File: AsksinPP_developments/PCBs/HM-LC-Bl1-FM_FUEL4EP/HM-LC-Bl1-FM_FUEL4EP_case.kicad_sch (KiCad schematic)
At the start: 34 parts, among them J1 Down button, J11 24V PSU, J12 230V supply relais, J13 Velux Motor, J14 Motor direction LEDs, J15 charge indication LED, J16 Cold_Device_Socket, J2 Up Button, J3 Dual LED, J4 Config Button, J6 Conn_01x02_Male, J7 LED rot, J8 LED grün, J9 LED gelb, M1 24V Velux Motor, SW1 Down Button, SW2 Down Button, SW3 Config Button

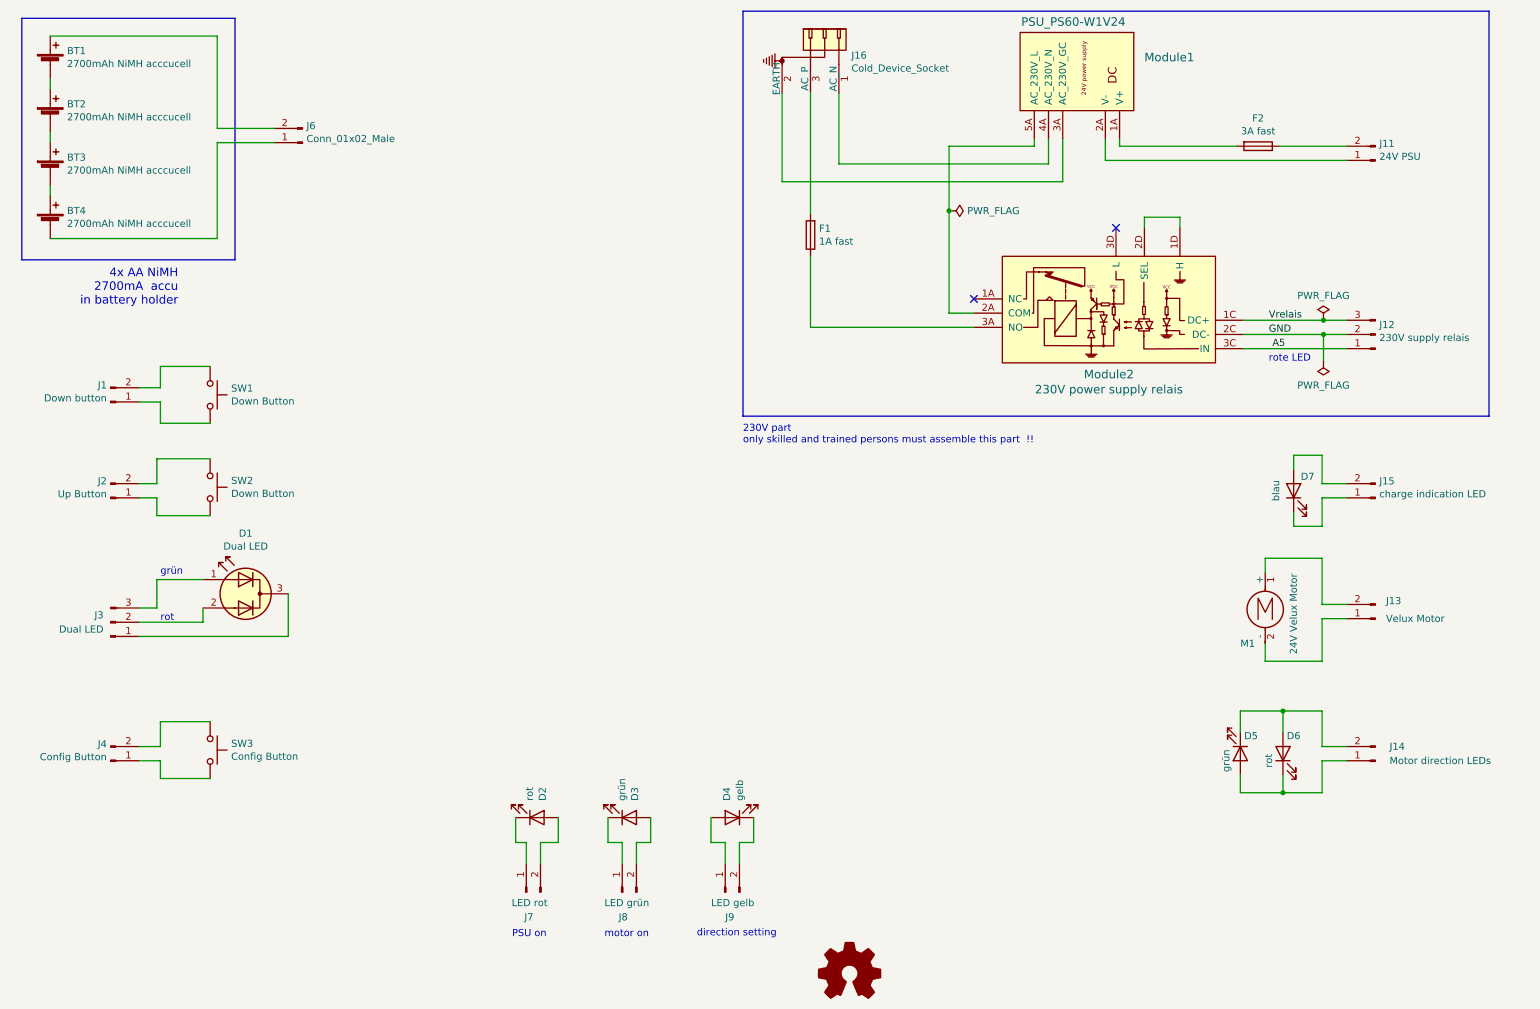
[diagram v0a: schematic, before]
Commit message: PCBs/HM-LC-Bl1-FM_FUEL4EP: migration to KiCAD 8
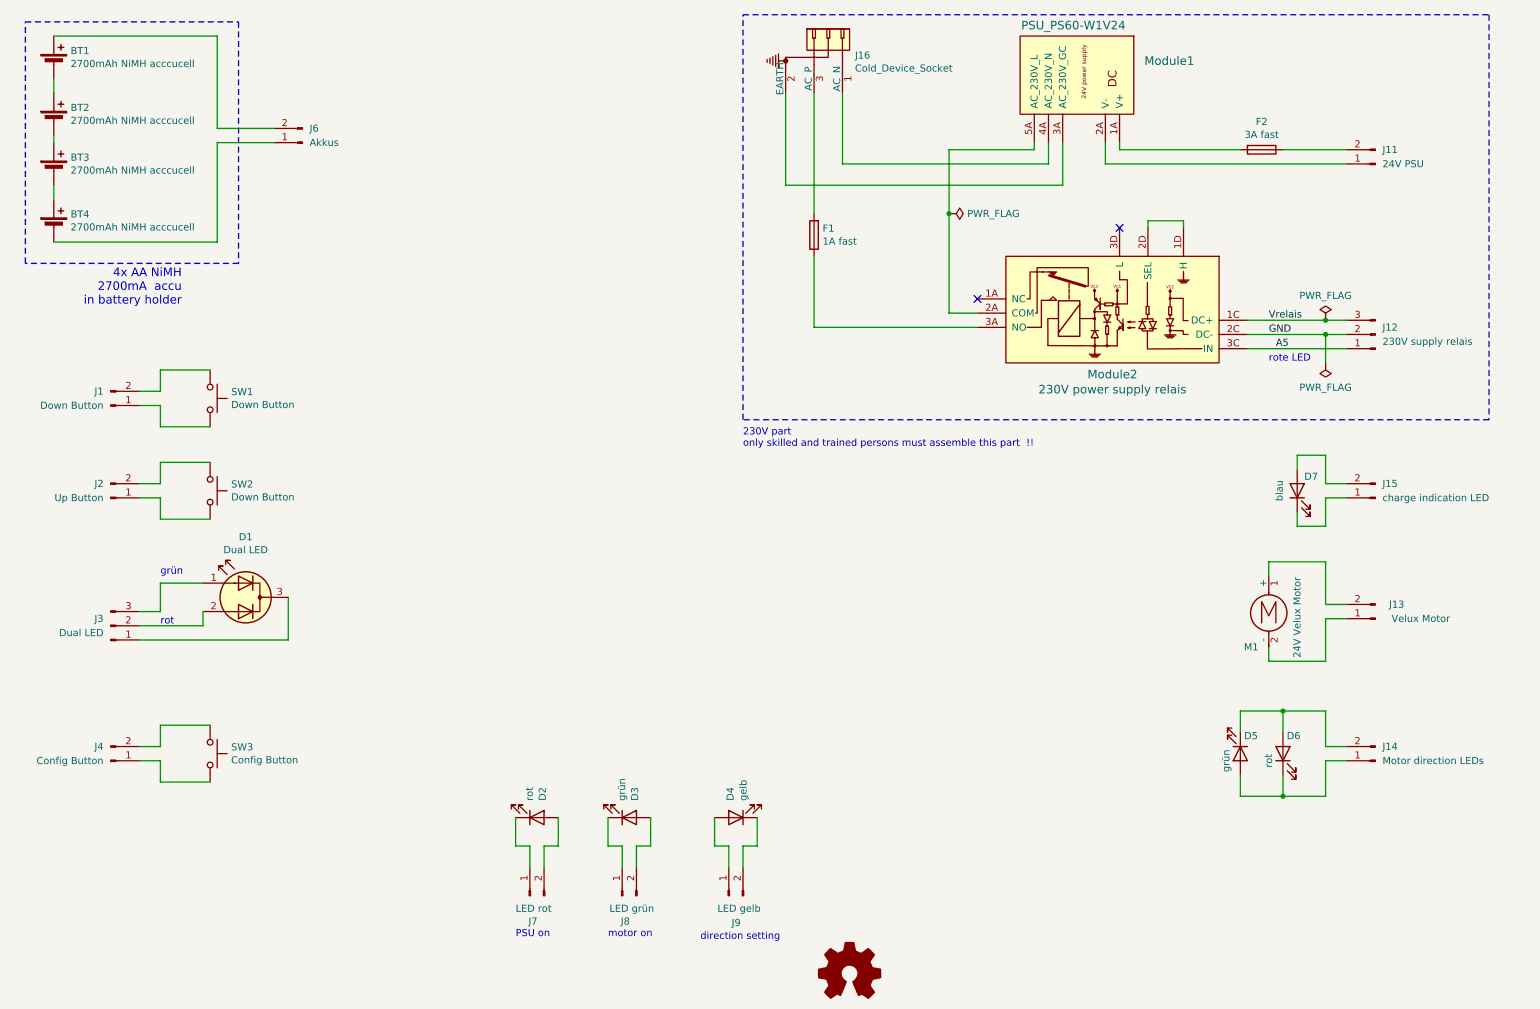
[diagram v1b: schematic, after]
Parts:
- removed J1: Down button, symbol Connector:Conn_01x02_Male
- removed J11: 24V PSU, symbol Connector:Conn_01x02_Male
- removed J12: 230V supply relais, symbol Connector:Conn_01x03_Male
- removed J13: Velux Motor, symbol Connector:Conn_01x02_Male
- removed J14: Motor direction LEDs, symbol Connector:Conn_01x02_Male
- removed J15: charge indication LED, symbol Connector:Conn_01x02_Male
- removed J2: Up Button, symbol Connector:Conn_01x02_Male
- removed J3: Dual LED, symbol Connector:Conn_01x03_Male
- removed J4: Config Button, symbol Connector:Conn_01x02_Male
- removed J6: Conn_01x02_Male, symbol Connector:Conn_01x02_Male
- removed J7: LED rot, symbol Connector:Conn_01x02_Male
- removed J8: LED grün, symbol Connector:Conn_01x02_Male
- removed J9: LED gelb, symbol Connector:Conn_01x02_Male
- added J1: Down Button, symbol Connector:Conn_01x02_Pin
- added J11: 24V PSU, symbol Connector:Conn_01x02_Pin
- added J12: 230V supply relais, symbol Connector:Conn_01x03_Pin
- added J13: Velux Motor, symbol Connector:Conn_01x02_Pin
- added J14: Motor direction LEDs, symbol Connector:Conn_01x02_Pin
- added J15: charge indication LED, symbol Connector:Conn_01x02_Pin
- added J2: Up Button, symbol Connector:Conn_01x02_Pin
- added J3: Dual LED, symbol Connector:Conn_01x03_Pin
- added J4: Config Button, symbol Connector:Conn_01x02_Pin
- added J6: Akkus, symbol Connector:Conn_01x02_Pin
- added J7: LED rot, symbol Connector:Conn_01x02_Pin
- added J8: LED grün, symbol Connector:Conn_01x02_Pin
- added J9: LED gelb, symbol Connector:Conn_01x02_Pin
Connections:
- net A5: now also J12.1 (Pin_1)
- net GND: now also J12.2 (Pin_2)
- net Vrelais: now also J12.3 (Pin_3)
- net at Module1.2A (V-): now also J11.1 (Pin_1)
- net at M1.1 (+): now also J13.2 (Pin_2)
- net at M1.2 (-): now also J13.1 (Pin_1)
- net at D5.2 (A), D6.1 (K): now also J14.1 (Pin_1)
- net at D5.1 (K), D6.2 (A): now also J14.2 (Pin_2)
- net at D2.1 (K): now also J7.1 (Pin_1)
- net at D2.2 (A): now also J7.2 (Pin_2)
- net at D3.1 (K): now also J8.1 (Pin_1)
- net at D3.2 (A): now also J8.2 (Pin_2)
- net at BT1.1 (+): now also J6.2 (Pin_2)
- net at BT4.2 (-): now also J6.1 (Pin_1)
- net at SW1.1: now also J1.2 (Pin_2)
- net at SW1.2: now also J1.1 (Pin_1)
- net at SW2.1: now also J2.2 (Pin_2)
- net at SW2.2: now also J2.1 (Pin_1)
- net at D1.1 (A1): now also J3.3 (Pin_3)
- net at D1.2 (A2): now also J3.2 (Pin_2)
- net at D1.3 (K): now also J3.1 (Pin_1)
- net at SW3.1: now also J4.2 (Pin_2)
- net at SW3.2: now also J4.1 (Pin_1)
- net at D4.1 (K): now also J9.2 (Pin_2)
- net at D4.2 (A): now also J9.1 (Pin_1)
- net at D7.1 (K): now also J15.1 (Pin_1)
- net at D7.2 (A): now also J15.2 (Pin_2)
- net at F2.1: now also J11.2 (Pin_2)
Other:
- moved on the sheet: BT1, BT2, BT3, BT4, D1, D4, D7, F1, F2, J16, M1, Module1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
